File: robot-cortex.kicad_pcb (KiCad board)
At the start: 2 copper layers, 71 parts, among them J1 USB4110GFA, Q1 SS8050-G, Q2 SS8050-G, U1 C2901617, U10 TPS63070, U11 TPS63070, U2 STM32G431CBT6, U3 TLE9250XSJXUMA1, U4 DF52-3S-0.8H(21), U5 DF52-4S-0.8H(21), U6 SPX3819M5-L-5-0, U7 DF52-5S-0.8H(21), U8 ESP32-WROOM-32E-H4, U9 CP2102N-A02-GQFN24R

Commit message: 3d models
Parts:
- added D7: C84264, robot-cortex:LED_0603_1608Metric, F.Cu at (180.8, 76.8)
- added M1: THRU_HOLE_PAD, robot-cortex:TEARDROP, F.Cu at (187.3, 78.1)
- added M2: THRU_HOLE_PAD, robot-cortex:TEARDROP, F.Cu at (191.2, 78.4)
- added R17: 470, robot-cortex:R_0402_1005Metric, F.Cu at (179.9, 79.0)
- U4: value DF52-3S-0.8H(21) -> DF52-5S-0.8H(21)
- U5: value DF52-4S-0.8H(21) -> DF52-5S-0.8H(21)
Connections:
- U8 pad 6: unconnected-(U8-IO34-Pad6) -> Net-(D7-A)

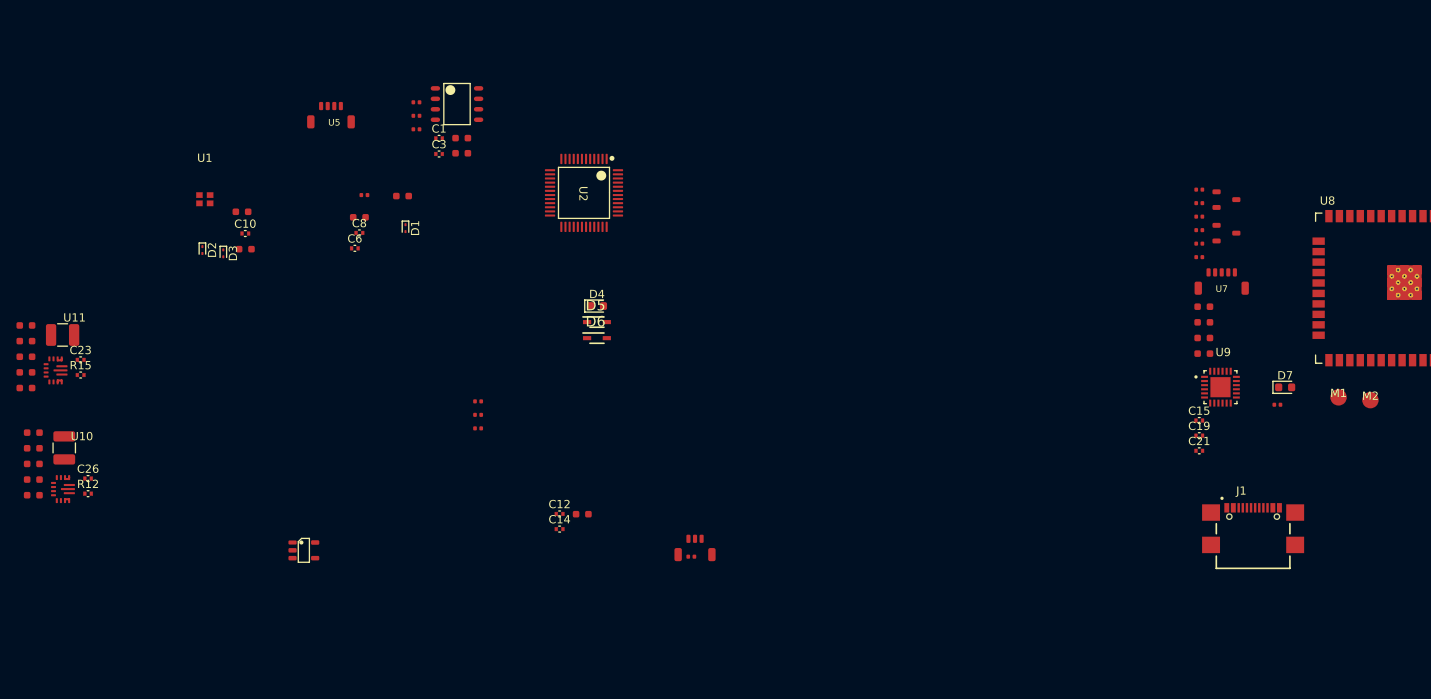
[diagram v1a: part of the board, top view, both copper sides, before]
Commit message: cannot route have to sleep but i will be back
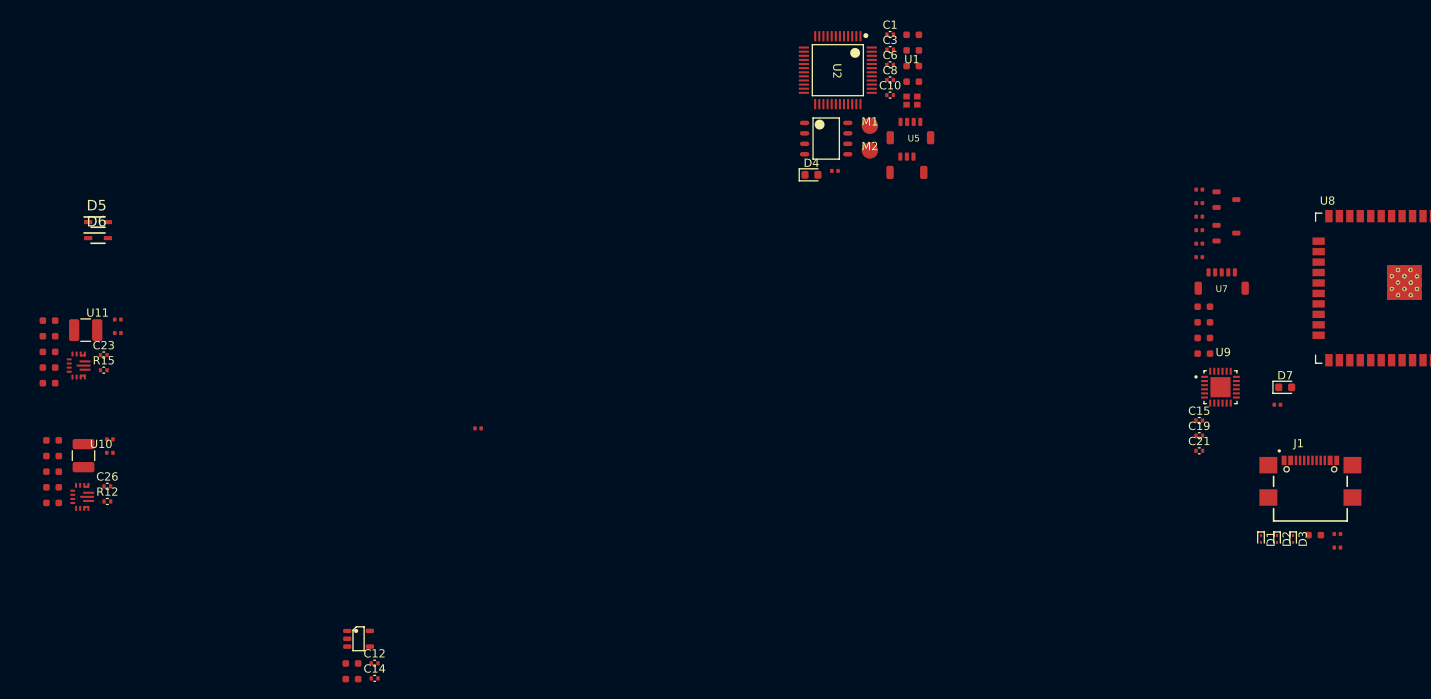
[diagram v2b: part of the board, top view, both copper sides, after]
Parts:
- moved D2 135.2 mm to (179.9, 95.3)
- moved D3 134.5 mm to (181.8, 95.3)
- moved R1 123.6 mm to (187.2, 94.7)
- moved R2 123.6 mm to (187.2, 96.3)
- moved C4 113.5 mm to (184.4, 94.8)
- moved D1 110.6 mm to (177.9, 95.3)
- moved U1 86.7 mm to (135.5, 42.0)
- moved C9 83.0 mm to (135.6, 39.7)
- moved C10 80.1 mm to (132.9, 41.3)
- moved R10 72.1 mm to (38.1, 83.2)
- moved U5 70.4 mm to (135.3, 44.6)
- moved C7 69.7 mm to (135.6, 37.8)
- moved C6 68.7 mm to (132.9, 37.7)
- moved M2 68.0 mm to (130.4, 48.1)
- moved C8 67.1 mm to (132.9, 39.5)
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
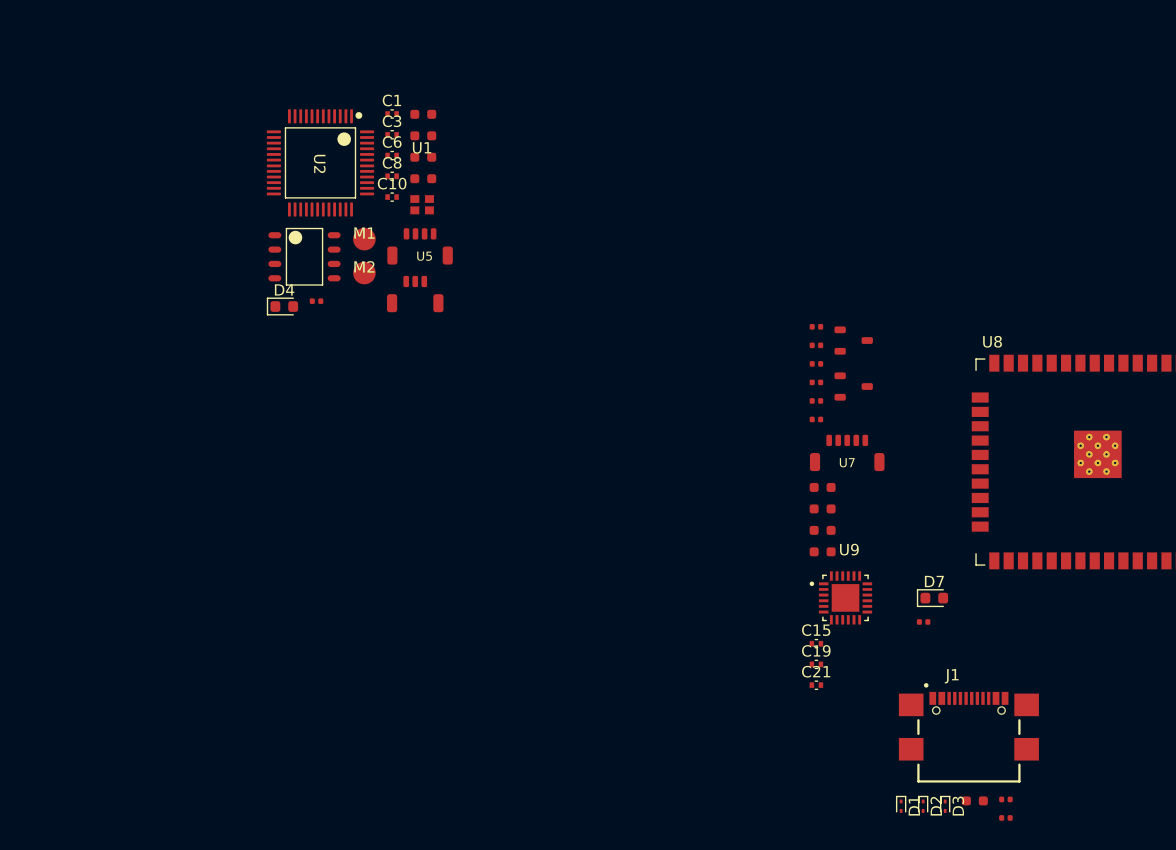
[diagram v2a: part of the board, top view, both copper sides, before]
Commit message: exposed boot and IO0 on jtag connector for esp32
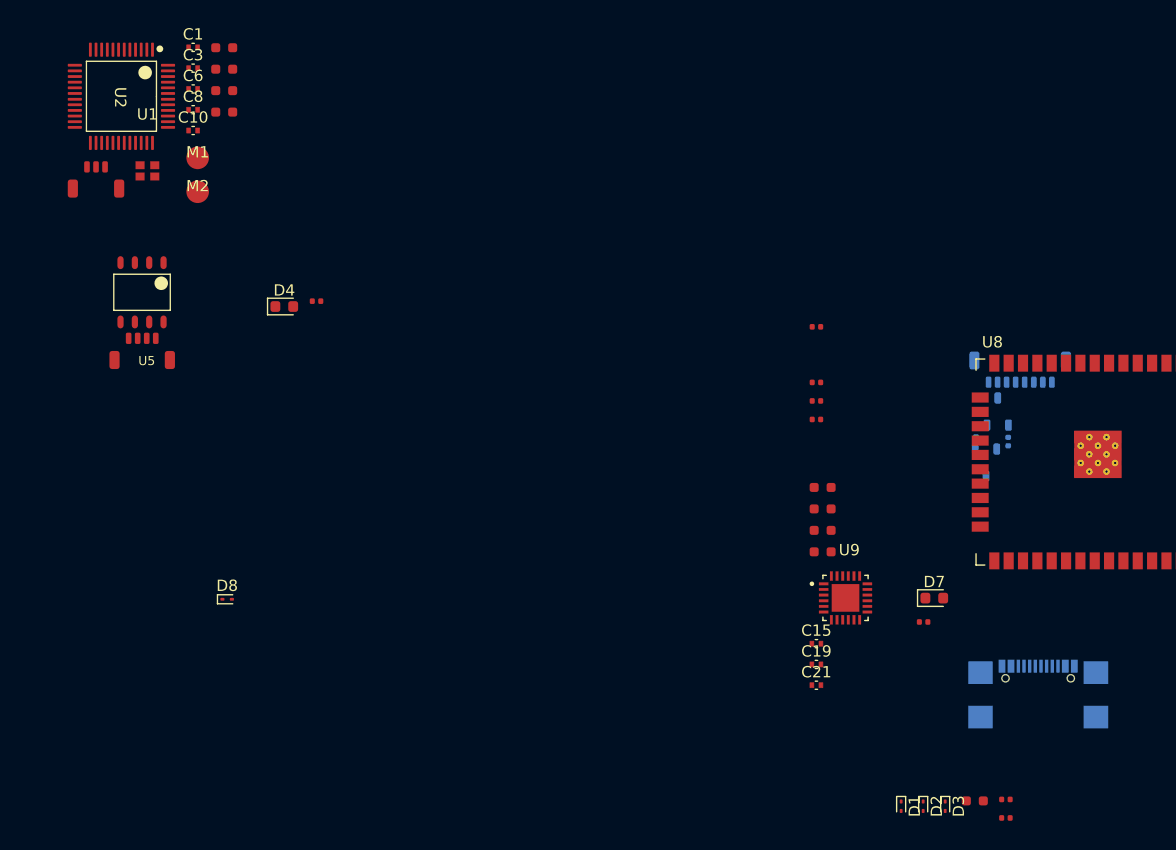
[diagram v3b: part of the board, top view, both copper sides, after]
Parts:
- added D8: ESD9B3.3ST5G, robot-cortex:D_SOD-923, F.Cu at (118.2, 77.0)
- J1, Q1, Q2, R5, R6: moved to B.Cu
- U4: value DF52-5S-0.8H(21) -> DF52-3S-0.8H(21)
- U5: value DF52-5S-0.8H(21) -> DF52-4S-0.8H(21)
- U7: footprint robot-cortex:DF52-5S-0.8H(21) -> robot-cortex:DF52-8S-0.8H(21); moved to B.Cu
- moved U4 30.0 mm to (106.6, 38.7)
- moved U5 26.3 mm to (110.7, 53.8)
- moved U1 24.5 mm to (111.2, 39.0)
- moved C1 18.6 mm to (115.2, 28.1)
- moved C10 18.6 mm to (115.2, 35.5)
- moved C2 18.6 mm to (118.0, 28.1)
- moved C3 18.6 mm to (115.2, 29.9)
- moved C5 18.6 mm to (118.0, 30.0)
- moved C6 18.6 mm to (115.2, 31.8)
- moved C7 18.6 mm to (118.0, 31.9)
- moved C8 18.6 mm to (115.2, 33.6)
- moved C9 18.6 mm to (118.0, 33.8)
- moved U2 18.6 mm to (108.9, 32.4)
- moved R6 18.3 mm to (187.4, 63.0), turned to 90 degrees
- moved M1 16.4 mm to (115.6, 37.9)
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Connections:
- U7 pad 1: /ESP32/TDO -> +3V3
- U7 pad 2: /ESP32/TMS -> /ESP32/EN
- U7 pad 3: /ESP32/TDI -> /ESP32/IO0
- U7 pad 4: /ESP32/TCK -> /ESP32/TDO
- U7 pad 5: GND -> /ESP32/TMS
- U7 pad 6: GND -> /ESP32/TDI
- U7 pad 7: GND -> /ESP32/TCK

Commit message: group layouts nearly done
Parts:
- removed R2: 5.1k, robot-cortex:R_0402_1005Metric
- C1, C10, C17, C18, C2, C20, C21, C3, C4, C5, C6, C7, C8, C9, D1, D2, D3, D4, M1, M2, R1, R3, R7, R8, R9, U1, U2, U3, U4, U5, U9: moved to B.Cu
- moved C13 100.6 mm to (164.8, 86.7), turned to -90 degrees
- moved R16 99.8 mm to (182.6, 81.7)
- moved C14 98.8 mm to (165.6, 86.6), turned to -90 degrees
- moved U6 96.2 mm to (162.2, 86.8)
- moved C11 95.1 mm to (159.6, 86.7), turned to -90 degrees
- moved C12 91.5 mm to (158.6, 86.7), turned to -90 degrees
- moved C19 43.0 mm to (202.1, 53.7)
- moved C15 38.7 mm to (198.6, 54.3), turned to 180 degrees
- moved U5 37.3 mm to (115.6, 16.9)
- moved C16 33.5 mm to (202.1, 54.5)
- moved C17 33.2 mm to (202.5, 58.5), turned to -90 degrees
- moved C18 32.8 mm to (201.4, 58.5), turned to -90 degrees
- moved R7 32.6 mm to (192.7, 81.6)
- moved R8 30.5 mm to (191.4, 81.6)
- moved R4 29.7 mm to (200.0, 54.3)
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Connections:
- J1 pad B5: Net-(J1-CC2) -> Net-(J1-CC1)
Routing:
- net /ESP32/CP210x_VBUS: track 0.00 -> 3.83 mm
- net +3V3: track 0.00 -> 3.19 mm
- net /D-: track 0.00 -> 2.56 mm
- net /D+: track 0.00 -> 2.56 mm
- net Net-(U11-L1): track 0.00 -> 2.45 mm
- net Net-(U11-L2): track 0.00 -> 2.41 mm
- net /VDD_MIXED: track 0.00 -> 2.35 mm
- net /LED: track 0.00 -> 1.44 mm
- net GND: track 0.00 -> 1.25 mm
- net Net-(U9-~{RST}): track 0.00 -> 1.04 mm
- net Net-(D4-K): track 0.00 -> 0.88 mm

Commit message: ground planes, more routing
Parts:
- added C34: C2998534, robot-cortex:C_0603_1608Metric, F.Cu at (146.3, 98.2)
- added C35: 100nF, robot-cortex:C_0402_1005Metric, F.Cu at (146.4, 97.2)
- moved C27 137.8 mm to (168.9, 88.4)
- moved C29 137.8 mm to (168.9, 87.3)
- moved C25 136.0 mm to (167.1, 81.8), turned to 180 degrees
- moved C30 135.4 mm to (166.4, 87.3), turned to 180 degrees
- moved C28 135.3 mm to (166.4, 88.4), turned to 180 degrees
- moved L2 135.3 mm to (170.2, 84.0)
- moved U10 132.8 mm to (167.3, 84.1)
- moved R10 129.0 mm to (167.0, 86.3), turned to 180 degrees
- moved C26 127.7 mm to (165.4, 84.9), turned to -90 degrees
- moved R11 127.6 mm to (165.7, 86.3), turned to 180 degrees
- moved R12 127.4 mm to (165.0, 83.8)
- moved C24 126.9 mm to (160.4, 102.1)
- moved C31 126.8 mm to (158.0, 102.1)
- moved L1 126.8 mm to (161.7, 97.8)
- moved R14 126.8 mm to (157.2, 100.1)
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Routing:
- net Net-(U11-L1): track 2.45 -> 0.00 mm
- net Net-(U11-L2): track 2.41 -> 0.00 mm
- net /VDD_MIXED: track 2.35 -> 4.75 mm
- net /SWDIO: track 0.00 -> 1.51 mm
- net /SWCLK: track 0.00 -> 1.50 mm
- net /PSU_TPS63070RNMR1/FB: track 0.00 -> 1.43 mm
- net /PSU_TPS63070RNMR/FB: track 0.00 -> 1.43 mm
- net Net-(U1-OUTPUT): track 0.00 -> 1.32 mm
- net GND: track 1.25 -> 2.50 mm
- net /NRST: track 0.00 -> 1.14 mm
- net Net-(U11-VAUX): track 0.00 -> 0.90 mm
- net Net-(U10-VAUX): track 0.00 -> 0.90 mm
- net Net-(U11-PG): track 0.00 -> 0.86 mm
- net Net-(U10-PG): track 0.00 -> 0.86 mm
- added copper zone on F.Cu, net +3V3
- added copper zone on F.Cu, net /+5V0
- added copper zone on F.Cu, net /VDD_MIXED
- added copper zone on B.Cu, net GND
- added copper zone on F.Cu, net GND
- added copper zone on F.Cu, net Net-(U10-L1)
- added copper zone on F.Cu, net Net-(U10-L2)
- added copper zone on F.Cu, net Net-(U11-L1)
- added copper zone on F.Cu, net Net-(U11-L2)

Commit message: placement mostly done and routing in progress
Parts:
- C34, C35, D5, D6: moved to B.Cu
- D4, R3, U4: moved to F.Cu
- moved R3 100.9 mm to (210.7, 115.9), turned to 0 degrees
- moved M2 99.2 mm to (215.5, 115.1), turned to 180 degrees
- moved D4 99.0 mm to (208.6, 115.9), turned to 180 degrees
- moved C10 97.1 mm to (208.1, 116.1), turned to 0 degrees
- moved M1 95.9 mm to (215.5, 112.6), turned to 180 degrees
- moved C7 94.4 mm to (204.1, 115.0)
- moved C1 93.5 mm to (213.8, 111.5), turned to -90 degrees
- moved C3 92.0 mm to (215.8, 109.4), turned to -90 degrees
- moved U1 91.2 mm to (214.5, 109.4), turned to -90 degrees
- moved U2 90.1 mm to (208.5, 110.8), turned to 180 degrees
- moved C9 88.9 mm to (197.4, 112.6), turned to 0 degrees
- moved C2 87.5 mm to (213.5, 107.0), turned to 0 degrees
- moved C6 86.3 mm to (213.5, 106.1), turned to 0 degrees
- moved C8 85.3 mm to (212.1, 105.8)
- moved U3 84.8 mm to (199.3, 109.3), turned to 180 degrees
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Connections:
- U8 pad 12: /BOOT -> unconnected-(U8-IO27-Pad12)
- U8 pad 36: unconnected-(U8-IO22-Pad36) -> /BOOT
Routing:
- net /ESP32/CP210x_RX: track 0.00 -> 20.9 mm, vias 0 -> 1
- net /ESP32/CP210x_TX: track 0.00 -> 17.8 mm, vias 0 -> 1
- net /NRST: track 1.14 -> 18.2 mm, vias 0 -> 1
- net /SPI1_MOSI: track 0.00 -> 14.3 mm, vias 0 -> 1
- net /UART2_TX: track 0.00 -> 12.3 mm, vias 0 -> 1
- net /UART2_RX: track 0.00 -> 11.1 mm, vias 0 -> 1
- net /SS: track 0.00 -> 11.1 mm, vias 0 -> 3
- net +3V3: track 3.19 -> 13.5 mm
- net /SPI1_SCK: track 0.00 -> 6.69 mm, vias 0 -> 1
- net /SPI1_MISO: track 0.00 -> 6.50 mm, vias 0 -> 1
- net /FDCAN1_RX: track 0.00 -> 3.73 mm
- net /FDCAN1_TX: track 0.00 -> 3.66 mm
- net /CANH: track 0.00 -> 1.91 mm
- net /CANL: track 0.00 -> 1.88 mm
- net Net-(D7-A): track 0.00 -> 1.66 mm
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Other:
- board outline added: 27.5 x 26.7 mm
- copper layers 2 -> 4

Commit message: lots of routing
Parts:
- moved U7 3.49 mm to (192.9, 100.3)
- moved U5 2.02 mm to (192.9, 109.4)
- moved D6 1.11 mm to (199.2, 103.5)
- moved C20 0.65 mm to (208.5, 100.7)
- moved R9 0.56 mm to (207.3, 101.9), turned to 90 degrees
- moved D1 0.51 mm to (204.7, 99.5)
- moved D2 0.51 mm to (203.1, 99.5)
- moved R1 0.51 mm to (198.4, 99.7)
- moved C21 0.51 mm to (208.3, 101.6)
- moved U9 0.51 mm to (203.9, 102.6)
- moved C4 0.51 mm to (200.8, 99.5)
- moved J1 0.51 mm to (203.9, 97.0)
- moved R7 0.51 mm to (206.7, 99.4)
- moved R8 0.51 mm to (208.0, 99.4)
- moved D3 0.47 mm to (200.4, 100.5)
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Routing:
- net +3V3: track 13.5 -> 97.0 mm, vias 0 -> 7
- net /ESP32/IO0: track 0.00 -> 40.0 mm, vias 0 -> 6
- net /ESP32/EN: track 0.00 -> 29.1 mm, vias 0 -> 3
- net /VDD_MIXED: track 4.75 -> 32.9 mm, vias 0 -> 4
- net /ESP32/DTR: track 0.00 -> 21.3 mm, vias 0 -> 2
- net /+5V0: track 0.00 -> 20.4 mm, vias 0 -> 2
- net /ESP32/RTS: track 0.00 -> 17.0 mm, vias 0 -> 3
- net /VBAT: track 0.00 -> 15.5 mm
- net /ESP32/TDO: track 0.00 -> 15.2 mm, vias 0 -> 2
- net /ESP32/TDI: track 0.00 -> 9.34 mm, vias 0 -> 1
- net /BOOT: track 0.00 -> 8.66 mm, vias 0 -> 1
- net /ESP32/TCK: track 0.00 -> 6.86 mm, vias 0 -> 1
- net /VUSB: track 0.00 -> 5.10 mm, vias 0 -> 1
- net /UART2_RX: track 11.1 -> 14.8 mm
- net /UART2_TX: track 12.3 -> 15.1 mm
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- added copper zone on B.Cu, net +3V3
- added copper zone on In1.Cu, net GND
- added copper zone on In2.Cu, net GND

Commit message: little more routing
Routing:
- net /ESP32/TMS: track 0.00 -> 12.7 mm, vias 0 -> 1
- net +3V3: track 97.0 -> 86.5 mm, vias 7 -> 9
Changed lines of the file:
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@@
   (segment (start 215.055 97.295) (end 214.43 97.92) (width 0.381) (layer "F.Cu") (net 1))
   (segment (start 214.555 93.94) (end 215.26 93.94) (width 0.3048) (layer "F.Cu") (net 1))
-  (segment (start 198.07 95.54) (end 203.17 100.64) (width 0.3048) (layer "F.Cu") (net 1))
   (segment (start 215.55 94.23) (end 215.46 94.14) (width 0.381) (layer "F.Cu") (net 1))
-  (segment (start 197.57 95.54) (end 198.07 95.54) (width 0.3048) (layer "F.Cu") (net 1))
-  (segment (start 203.17 100.64) (end 206 100.64) (width 0.3048) (layer "F.Cu") (net 1))
   (segment (start 215.26 93.94) (end 215.46 94.14) (width 0.3048) (layer "F.Cu") (net 1))
   (segment (start 213.08 105.37) (end 213.9 105.37) (width 0.381) (layer "F.Cu") (net 1))
@@
   (via (at 207.410803 100.0785) (size 0.45) (drill 0.2) (layers "F.Cu" "B.Cu") (net 1))
   (via (at 213.08 105.37) (size 0.45) (drill 0.2) (layers "F.Cu" "B.Cu") (net 1))
+  (via (at 194.92 90.23) (size 0.45) (drill 0.2) (layers "F.Cu" "B.Cu") (net 1))
   (via (at 213.9 105.37) (size 0.45) (drill 0.2) (layers "F.Cu" "B.Cu") (net 1))
+  (via (at 194.01 92.77) (size 0.45) (drill 0.2) (layers "F.Cu" "B.Cu") (net 1))
   (via (at 211.53 107.84) (size 0.45) (drill 0.2) (layers "F.Cu" "B.Cu") (net 1))
   (segment (start 206.66 108.42) (end 210.95 108.42) (width 0.254) (layer "In1.Cu") (net 1))
@@
   (segment (start 206.66 100.05) (end 207.065 99.645) (width 0.254) (layer "B.Cu") (net 9))
   (segment (start 206.362878 101.86) (end 206.66 101.562878) (width 0.254) (layer "B.Cu") (net 9))
+  (segment (start 201.58 95.25755) (end 201.58 95.65) (width 0.254) (layer "F.Cu") (net 10))
+  (segment (start 196.73 99.13) (end 198.7 97.16) (width 0.254) (layer "F.Cu") (net 10))
+  (segment (start 198.7 95.31) (end 199.437 94.573) (width 0.254) (layer "F.Cu") (net 10))
+  (segment (start 200.89545 94.573) (end 201.58 95.25755) (width 0.254) (layer "F.Cu") (net 10))
+  (segment (start 199.437 94.573) (end 200.89545 94.573) (width 0.254) (layer "F.Cu") (net 10))
+  (segment (start 198.7 97.16) (end 198.7 95.31) (width 0.254) (layer "F.Cu") (net 10))
+  (via (at 196.73 99.13) (size 0.45) (drill 0.2) (layers "F.Cu" "B.Cu") (net 10))
+  (segment (start 192.88 99.91) (end 195.95 99.91) (width 0.254) (layer "B.Cu") (net 10))
+  (segment (start 195.95 99.91) (end 196.73 99.13) (width 0.254) (layer "B.Cu") (net 10))
   (segment (start 199.34 95.71) (end 200.25 95.71) (width 0.254) (layer "F.Cu") (net 11))
   (segment (start 200.25 95.71) (end 200.31 95.65) (width 0.254) (layer "F.Cu") (net 11))
